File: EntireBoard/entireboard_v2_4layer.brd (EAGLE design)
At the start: 60 x 60 mm, 52 parts, among them J1 FTSH-105-01-XXX-DV-K, P1 0532610271, U1 YKA, U2 RHD2216_QFN

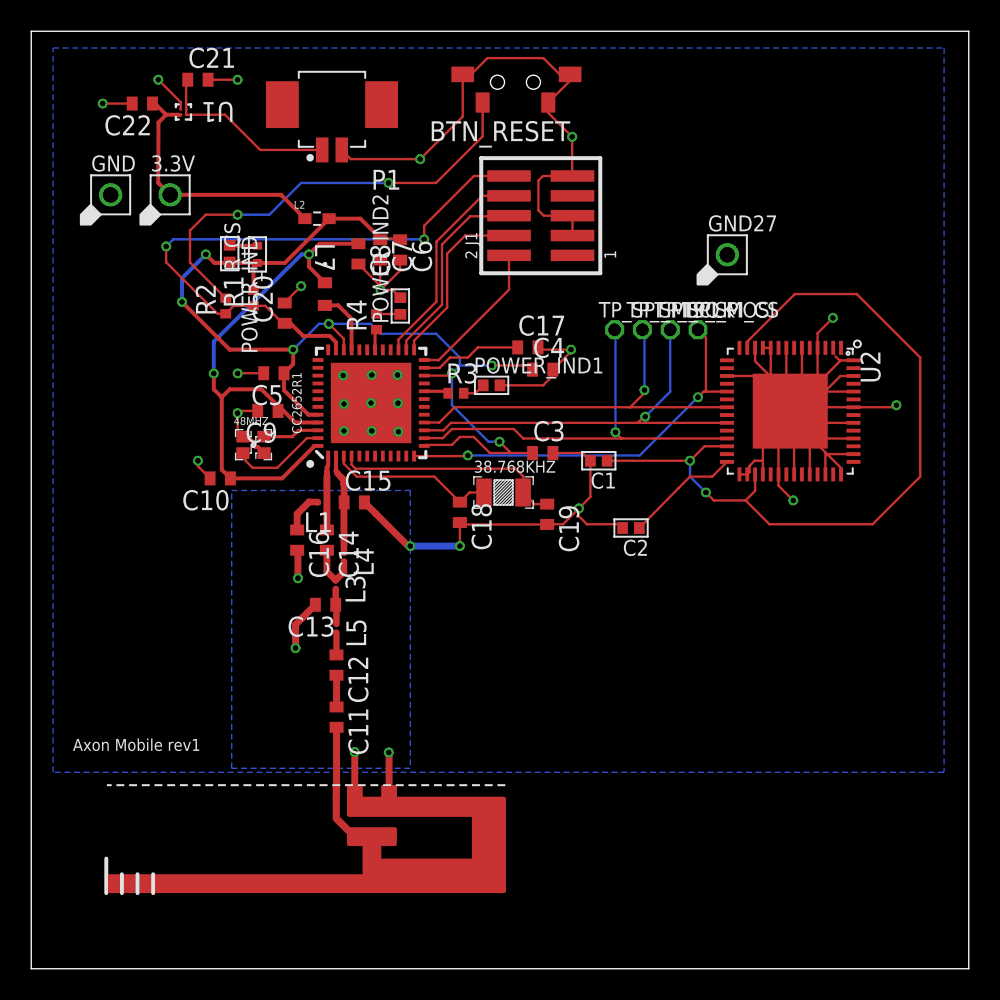
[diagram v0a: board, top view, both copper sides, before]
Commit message: drc for 4-layer
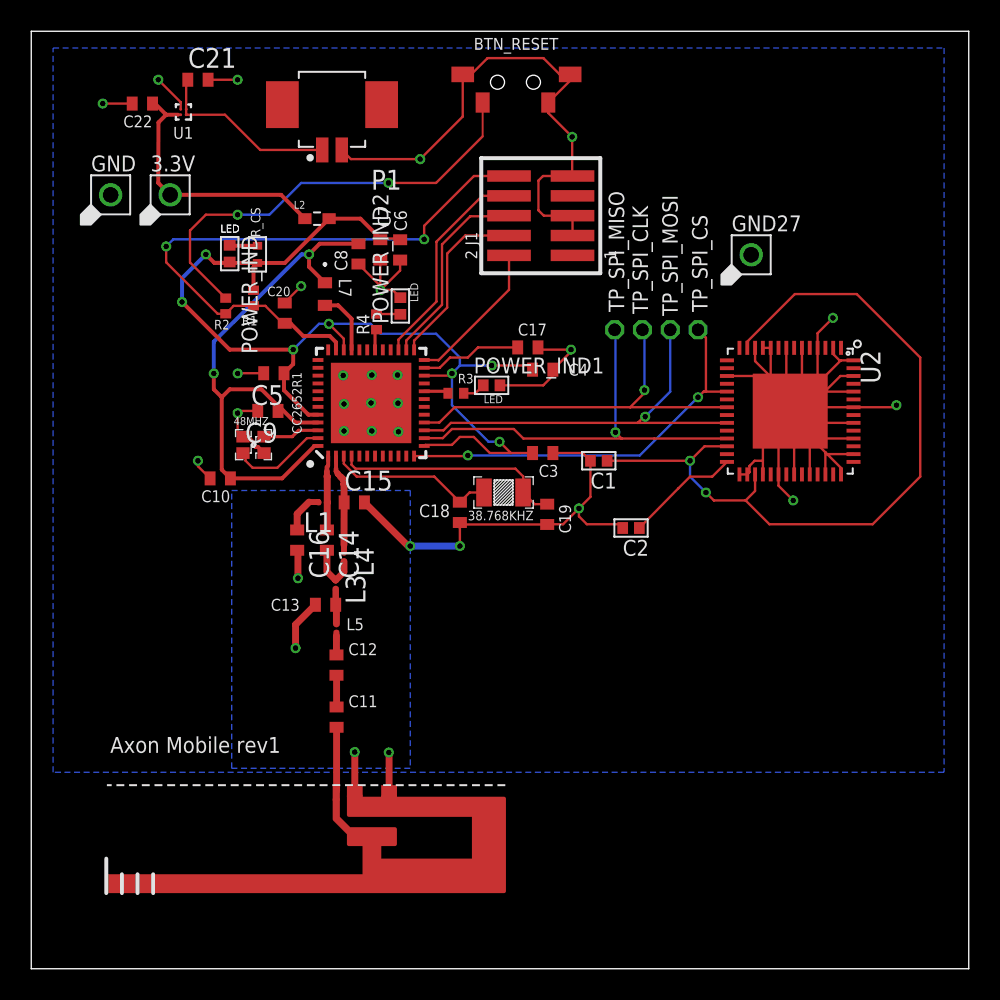
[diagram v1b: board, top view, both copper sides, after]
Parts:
- moved GND27 1.52 mm to (46.1, 45.7)
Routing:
- net GND: track 174.9 -> 175.5 mm, vias 22 -> 30
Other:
- board text added: "LED"
